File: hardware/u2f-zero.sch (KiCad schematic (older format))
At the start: 13 parts, among them SW1 SW_PUSH

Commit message: add part references
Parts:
- A1: Distributer Link (none) -> http://www.digikey.com/product-detail/en/atmel/ATECC508A-SS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; Distributer PN (none) -> ATECC508A-SSHDA-B-ND; MFG Name (none) -> Atmel; MFG Part Num (none) -> ATECC508A-SSHDA-B
- C3: Distributer Link (none) -> http://www.digikey.com/product-detail/en/CL05A104MP5NNNC/12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; Distributer PN (none) -> 1276-1443-1-ND; MFG Name (none) -> Samsung Electro-Mechanics America, Inc; MFG Part Num (none) -> CL05A104MP5NNNC
- C4: Distributer Link (none) -> http://www.digikey.com/product-detail/en/CL10B475KQ8NQNC/12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; Distributer PN (none) -> 1276-2087-1-ND; MFG Name (none) -> Samsung Electro-Mechanics America, Inc; MFG Part Num (none) -> CL10B475KQ8NQNC
- E0: Distributer Link (none) -> http://www.digikey.com/product-detail/en/silicon-labs/EFM8U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; Distributer PN (none) -> r 336-3411-5-ND; MFG Name (none) -> Silicon Labs; MFG Part Num (none) -> EFM8UB11F16G-C-QSOP24
- R1: Distributer Link (none) -> http://www.digikey.com/product-detail/en/CRCW0603100RFKEA/5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; Distributer PN (none) -> 541-100HCT-ND; MFG Name (none) -> Vishay Dale; MFG Part Num (none) -> CRCW0603100RFKEA
- RGB1: Distributer Link (none) -> http://www.digikey.com/product-detail/en/LTST-C19HE1WT/160-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; Distributer PN (none) -> 160-2162-1-ND; MFG Name (none) -> Lite-On Inc; MFG Part Num (none) -> LTST-C19HE1WT
- SW1: Distributer Link (none) -> http://www.digikey.com/product-detail/en/e-switch/TL3305AF2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; Distributer PN (none) -> EG5353CT-ND; MFG Name (none) -> E-Switch; MFG Part Num (none) -> TL3305AF260QG
- Z1: Distributer Link (none) -> http://www.digikey.com/product-detail/en/DF5A5.6JE,LM/DF5A5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; Distributer PN (none) -> DF5A5.6JELMCT-ND; MFG Name (none) -> Toshiba Semiconductor and Storage; MFG Part Num (none) -> DF5A5.6JE,LM
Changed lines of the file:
@@
 F 2 "Housings_SOIC:SOIC-8_3.9x4.9mm_Pitch1.27mm" H 4700 3300 60  0001 C CNN
 F 3 "http://www.atmel.com/Images/Atmel-8923S-CryptoAuth-ATECC508A-Datasheet-Summary.pdf" H 4700 3300 60  0001 C CNN
+F 4 "Atmel" H 5100 3050 60  0001 C CNN "MFG Name"
+F 5 "ATECC508A-SSHDA-B" H 5100 3050 60  0001 C CNN "MFG Part Num"
+F 6 "ATECC508A-SSHDA-B-ND" H 5100 3050 60  0001 C CNN "Distributer PN"
+F 7 "http://www.digikey.com/product-detail/en/atmel/ATECC508A-SSHDA-B/ATECC508A-SSHDA-B-ND/5213053" H 5100 3050 60  0001 C CNN "Distributer Link"
 	1    5100 3050
 	-1   0    0    1
@@
 F 2 "Capacitors_SMD:C_0402" H 5338 5600 50  0001 C CNN
 F 3 "http://media.digikey.com/pdf/Data%20Sheets/Samsung%20PDFs/CL_Series_MLCC_ds.pdf" H 5300 5750 50  0001 C CNN
+F 4 "Samsung Electro-Mechanics America, Inc" H 5300 5750 60  0001 C CNN "MFG Name"
+F 5 "CL05A104MP5NNNC" H 5300 5750 60  0001 C CNN "MFG Part Num"
+F 6 "1276-1443-1-ND" H 5300 5750 60  0001 C CNN "Distributer PN"
+F 7 "http://www.digikey.com/product-detail/en/CL05A104MP5NNNC/1276-1443-1-ND/3889529" H 5300 5750 60  0001 C CNN "Distributer Link"
 	1    5300 5750
 	0    -1   1    0
@@
 F 2 "Capacitors_SMD:C_0603" H 5338 5950 50  0001 C CNN
 F 3 "http://media.digikey.com/pdf/Data%20Sheets/Samsung%20PDFs/CL_Series_MLCC_ds.pdf" H 5300 6100 50  0001 C CNN
+F 4 "Samsung Electro-Mechanics America, Inc" H 5300 6100 60  0001 C CNN "MFG Name"
+F 5 "CL10B475KQ8NQNC" H 5300 6100 60  0001 C CNN "MFG Part Num"
+F 6 "1276-2087-1-ND" H 5300 6100 60  0001 C CNN "Distributer PN"
+F 7 "http://www.digikey.com/product-detail/en/CL10B475KQ8NQNC/1276-2087-1-ND/3890173" H 5300 6100 60  0001 C CNN "Distributer Link"
 	1    5300 6100
 	0    1    1    0
@@
 F 2 "TO_SOT_Packages_SMD:SOT-553" H 3250 3950 60  0001 C CNN
 F 3 "http://optoelectronics.liteon.com/upload/download/DS22-2008-0044/S_110_LTST-C19HE1WT.pdf" H 3250 3950 60  0001 C CNN
+F 4 "Toshiba Semiconductor and Storage" H 3250 3950 60  0001 C CNN "MFG Name"
+F 5 "DF5A5.6JE,LM" H 3250 3950 60  0001 C CNN "MFG Part Num"
+F 6 "DF5A5.6JELMCT-ND" H 3250 3950 60  0001 C CNN "Distributer PN"
+F 7 "http://www.digikey.com/product-detail/en/DF5A5.6JE,LM/DF5A5.6JELMCT-ND/5403466" H 3250 3950 60  0001 C CNN "Distributer Link"
 	1    3250 3950
 	1    0    0    -1
@@
 F 2 "Resistors_SMD:R_0603" V 8030 4900 50  0001 C CNN
 F 3 "http://www.vishay.com/docs/20035/dcrcwe3.pdf" H 8100 4900 50  0001 C CNN
+F 4 "Vishay Dale" H 8100 4900 60  0001 C CNN "MFG Name"
+F 5 "CRCW0603100RFKEA" H 8100 4900 60  0001 C CNN "MFG Part Num"
+F 6 "541-100HCT-ND" H 8100 4900 60  0001 C CNN "Distributer PN"
+F 7 "http://www.digikey.com/product-detail/en/CRCW0603100RFKEA/541-100HCT-ND/1179695" H 8100 4900 60  0001 C CNN "Distributer Link"
 	1    8100 4900
 	-1   0    0    1
@@
 F 2 "footprints:LED-0606" H 7850 4750 60  0001 C CNN
 F 3 "http://optoelectronics.liteon.com/upload/download/DS22-2008-0044/S_110_LTST-C19HE1WT.pdf" H 7050 4750 60  0001 C CNN
+F 4 "Lite-On Inc" H 7050 4700 60  0001 C CNN "MFG Name"
+F 5 "LTST-C19HE1WT" H 7050 4700 60  0001 C CNN "MFG Part Num"
+F 6 "160-2162-1-ND" H 7050 4700 60  0001 C CNN "Distributer PN"
+F 7 "http://www.digikey.com/product-detail/en/LTST-C19HE1WT/160-2162-1-ND/4866310" H 7050 4700 60  0001 C CNN "Distributer Link"
 	1    7050 4700
 	1    0    0    1
@@
 F 2 "footprints:u2f-button" H 6500 5200 50  0001 C CNN
 F 3 "http://www.digikey.com/product-detail/en/e-switch/TL3305AF260QG/EG5353CT-ND/5816198" H 6500 5200 50  0001 C CNN
+F 4 "E-Switch" H 6500 5200 60  0001 C CNN "MFG Name"
+F 5 "TL3305AF260QG" H 6500 5200 60  0001 C CNN "MFG Part Num"
+F 6 "EG5353CT-ND" H 6500 5200 60  0001 C CNN "Distributer PN"
+F 7 "http://www.digikey.com/product-detail/en/e-switch/TL3305AF260QG/EG5353CT-ND/5816198" H 6500 5200 60  0001 C CNN "Distributer Link"
 	1    6500 5200
 	1    0    0    -1
@@
 F 2 "footprints:QSOP-24_3.9x8.7mm_Pitch0.635mm_fat" H 5650 4650 60  0001 C CNN
 F 3 "https://www.silabs.com/Support%20Documents/TechnicalDocs/EFM8UB1_DataSheet.pdf" H 5350 4250 60  0001 C CNN
+F 4 "Silicon Labs" H 5350 4250 60  0001 C CNN "MFG Name"
+F 5 "EFM8UB11F16G-C-QSOP24" H 5350 4250 60  0001 C CNN "MFG Part Num"
+F 6 "r	336-3411-5-ND" H 5350 4250 60  0001 C CNN "Distributer PN"
+F 7 "http://www.digikey.com/product-detail/en/silicon-labs/EFM8UB11F16G-C-QSOP24/336-3411-5-ND/5592439" H 5350 4250 60  0001 C CNN "Distributer Link"
 	1    5350 4250
 	1    0    0    -1

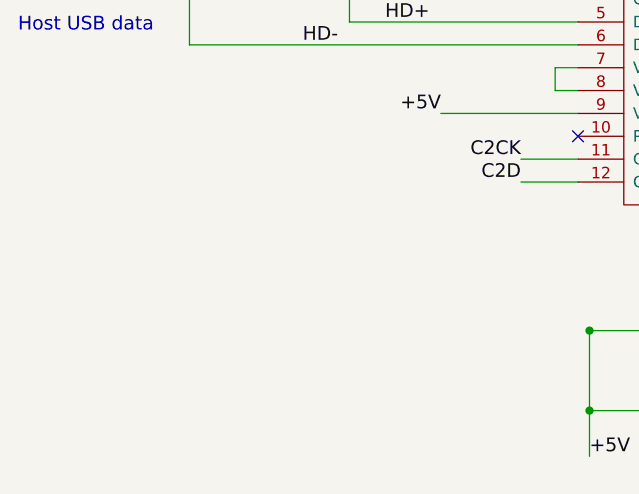
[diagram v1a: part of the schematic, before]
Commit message: add fiducials
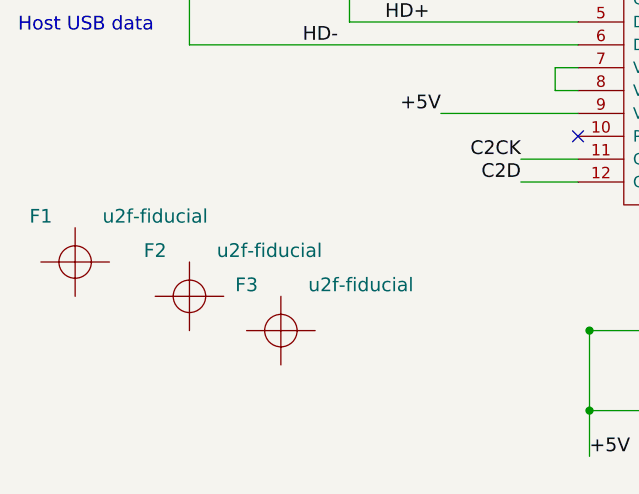
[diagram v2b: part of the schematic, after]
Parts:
- added F1, F2, F3: u2f-fiducial, footprints:u2f-fiducial, symbol u2f-fiducial
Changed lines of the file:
@@
 Wire Wire Line
 	4700 4700 4700 4600
+$Comp
+L u2f-fiducial F1
+U 1 1 571C39BB
+P 2600 5450
+F 0 "F1" H 2450 5650 60  0000 C CNN
+F 1 "u2f-fiducial" H 2950 5650 60  0000 C CNN
+F 2 "footprints:u2f-fiducial" H 2600 5450 60  0001 C CNN
+F 3 "" H 2600 5450 60  0000 C CNN
+	1    2600 5450
+	1    0    0    -1
+$EndComp
+$Comp
+L u2f-fiducial F2
+U 1 1 571C3A1E
+P 3100 5600
+F 0 "F2" H 2950 5800 60  0000 C CNN
+F 1 "u2f-fiducial" H 3450 5800 60  0000 C CNN
+F 2 "footprints:u2f-fiducial" H 3100 5600 60  0001 C CNN
+F 3 "" H 3100 5600 60  0000 C CNN
+	1    3100 5600
+	1    0    0    -1
+$EndComp
+$Comp
+L u2f-fiducial F3
+U 1 1 571C3A85
+P 3500 5750
+F 0 "F3" H 3350 5950 60  0000 C CNN
+F 1 "u2f-fiducial" H 3850 5950 60  0000 C CNN
+F 2 "footprints:u2f-fiducial" H 3500 5750 60  0001 C CNN
+F 3 "" H 3500 5750 60  0000 C CNN
+	1    3500 5750
+	1    0    0    -1
+$EndComp
 $EndSCHEMATC

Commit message: Replace tiny schematic/netlist parts with larger parts.
All passive components: standardized on 0805
TVS diode: currently TSOT-23-5 (could become 6 pins)
LED: 0606 => 5050 (8.3x the horizontal linear size)
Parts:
- C3: footprint Capacitors_SMD:C_0402 -> Capacitors_SMD:C_0805
- C4: footprint Capacitors_SMD:C_0603 -> Capacitors_SMD:C_0805
- R1: footprint Resistors_SMD:R_0603 -> Resistors_SMD:R_0805
- RGB1: footprint footprints:LED-0606 -> LEDs:LED_RGB_5050-6
- Z1: footprint TO_SOT_Packages_SMD:SOT-553 -> TO_SOT_Packages_SMD:TSOT-23-5
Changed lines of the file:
@@
 F 0 "C3" H 5325 5850 50  0000 L CNN
 F 1 "0.1uF" H 5325 5650 50  0000 L CNN
-F 2 "Capacitors_SMD:C_0402" H 5338 5600 50  0001 C CNN
+F 2 "Capacitors_SMD:C_0805" H 5338 5600 50  0001 C CNN
 F 3 "http://media.digikey.com/pdf/Data%20Sheets/Samsung%20PDFs/CL_Series_MLCC_ds.pdf" H 5300 5750 50  0001 C CNN
 F 4 "Samsung Electro-Mechanics America, Inc" H 5300 5750 60  0001 C CNN "MFG Name"
@@
 F 0 "C4" H 5325 6200 50  0000 L CNN
 F 1 "4.7uF" H 5325 6000 50  0000 L CNN
-F 2 "Capacitors_SMD:C_0603" H 5338 5950 50  0001 C CNN
+F 2 "Capacitors_SMD:C_0805" H 5338 5950 50  0001 C CNN
 F 3 "http://media.digikey.com/pdf/Data%20Sheets/Samsung%20PDFs/CL_Series_MLCC_ds.pdf" H 5300 6100 50  0001 C CNN
 F 4 "Samsung Electro-Mechanics America, Inc" H 5300 6100 60  0001 C CNN "MFG Name"
@@
 F 0 "Z1" H 2850 4000 60  0000 C CNN
 F 1 "DF5A5.6JE" H 2700 4100 60  0000 C CNN
-F 2 "TO_SOT_Packages_SMD:SOT-553" H 3250 3950 60  0001 C CNN
+F 2 "TO_SOT_Packages_SMD:TSOT-23-5" H 3250 3950 60  0001 C CNN
 F 3 "http://optoelectronics.liteon.com/upload/download/DS22-2008-0044/S_110_LTST-C19HE1WT.pdf" H 3250 3950 60  0001 C CNN
 F 4 "Toshiba Semiconductor and Storage" H 3250 3950 60  0001 C CNN "MFG Name"
@@
 F 0 "R1" V 8180 4900 50  0000 C CNN
 F 1 "100" V 8100 4900 50  0000 C CNN
-F 2 "Resistors_SMD:R_0603" V 8030 4900 50  0001 C CNN
+F 2 "Resistors_SMD:R_0805" V 8030 4900 50  0001 C CNN
 F 3 "http://www.vishay.com/docs/20035/dcrcwe3.pdf" H 8100 4900 50  0001 C CNN
 F 4 "Vishay Dale" H 8100 4900 60  0001 C CNN "MFG Name"
@@
 F 0 "RGB1" H 7300 4850 60  0000 C CNN
 F 1 "CA_RGB" H 6950 4850 60  0000 C CNN
-F 2 "footprints:LED-0606" H 7850 4750 60  0001 C CNN
+F 2 "LEDs:LED_RGB_5050-6" H 7850 4750 60  0001 C CNN
 F 3 "http://optoelectronics.liteon.com/upload/download/DS22-2008-0044/S_110_LTST-C19HE1WT.pdf" H 7050 4750 60  0001 C CNN
 F 4 "Lite-On Inc" H 7050 4700 60  0001 C CNN "MFG Name"

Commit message: Update for actual physical LED/TVS parts chosen
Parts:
- RGB1: footprint LEDs:LED_RGB_5050-6 -> LEDs:LED_Cree-PLCC4_3.2x2.8mm_CCW; symbol CA_RGB-RESCUE-u2f-zero -> CA_RGB-RESCUE-u2f-zero__Cree
- Z1: footprint TO_SOT_Packages_SMD:TSOT-23-5 -> TO_SOT_Packages_SMD:SOT-353_SC-70-5
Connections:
- net at R1.2: now also RGB1.2 (VCC); no longer RGB1.4 (VCC)
- net at E0.19 (P1.0): now also RGB1.4 (G); no longer RGB1.2 (G)
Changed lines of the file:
@@
 F 0 "Z1" H 2850 4000 60  0000 C CNN
 F 1 "DF5A5.6JE" H 2700 4100 60  0000 C CNN
-F 2 "TO_SOT_Packages_SMD:TSOT-23-5" H 3250 3950 60  0001 C CNN
+F 2 "TO_SOT_Packages_SMD:SOT-353_SC-70-5" H 3250 3950 60  0001 C CNN
 F 3 "http://optoelectronics.liteon.com/upload/download/DS22-2008-0044/S_110_LTST-C19HE1WT.pdf" H 3250 3950 60  0001 C CNN
 F 4 "Toshiba Semiconductor and Storage" H 3250 3950 60  0001 C CNN "MFG Name"
@@
 Secure element for EC
 $Comp
-L CA_RGB-RESCUE-u2f-zero RGB1
+L CA_RGB-RESCUE-u2f-zero__Cree RGB1
 U 1 1 5686DEFD
 P 7050 4700
 F 0 "RGB1" H 7300 4850 60  0000 C CNN
 F 1 "CA_RGB" H 6950 4850 60  0000 C CNN
-F 2 "LEDs:LED_RGB_5050-6" H 7850 4750 60  0001 C CNN
+F 2 "LEDs:LED_Cree-PLCC4_3.2x2.8mm_CCW" H 7850 4750 60  0001 C CNN
 F 3 "http://optoelectronics.liteon.com/upload/download/DS22-2008-0044/S_110_LTST-C19HE1WT.pdf" H 7050 4750 60  0001 C CNN
 F 4 "Lite-On Inc" H 7050 4700 60  0001 C CNN "MFG Name"

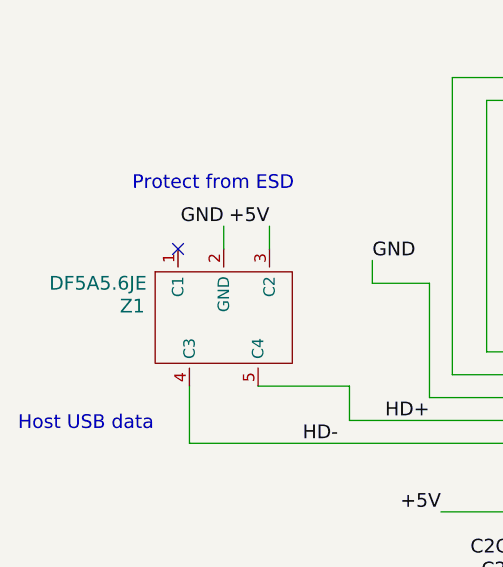
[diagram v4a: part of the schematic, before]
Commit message: Update the BOM csv with new values matching the larger footprints
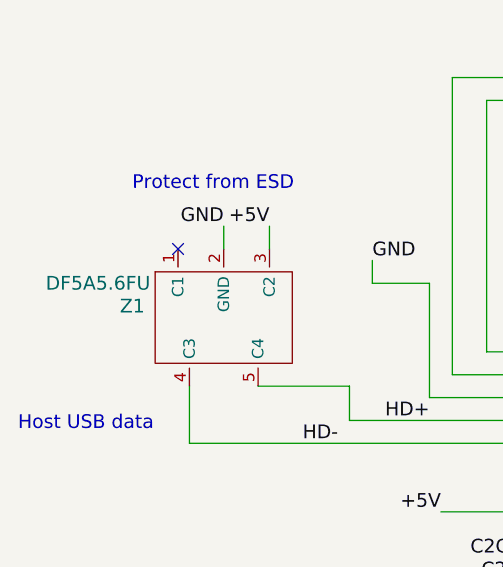
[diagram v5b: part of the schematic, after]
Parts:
- C3: Distributer Link http://www.digikey.com/product-detail/en/CL05A104MP5NNNC/12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 -> https://www.digikey.com/product-detail/en/murata-electronic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; Distributer PN 1276-1443-1-ND -> 490-12558-1-ND; MFG Name Samsung Electro-Mechanics America, Inc -> Murata Manufacturing Co., Ltd.; MFG Part Num CL05A104MP5NNNC -> GRM219R71C104MA01J
- C4: Distributer Link http://www.digikey.com/product-detail/en/CL10B475KQ8NQNC/12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 -> https://www.digikey.com/product-detail/en/murata-electronic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; Distributer PN 1276-2087-1-ND -> 490-14466-1-ND; MFG Name Samsung Electro-Mechanics America, Inc -> Murata Manufacturing Co., Ltd.; MFG Part Num CL10B475KQ8NQNC -> GRM21BR71C475KE51L
- R1: Distributer Link http://www.digikey.com/product-detail/en/CRCW0603100RFKEA/5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 -> https://www.digikey.com/product-detail/en/vishay-dale/CRCW0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; Distributer PN 541-100HCT-ND -> 541-100CCT-ND; MFG Part Num CRCW0603100RFKEA -> CRCW0805100RFKEA
- RGB1: Distributer Link http://www.digikey.com/product-detail/en/LTST-C19HE1WT/160-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 -> https://www.digikey.com/product-detail/en/cree-inc/CLVBA-FK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; Distributer PN 160-2162-1-ND -> CLVBA-FKA-CAEDH8BBB7A363CT-ND; MFG Name Lite-On Inc -> Cree; MFG Part Num LTST-C19HE1WT -> CLVBA-FKA
- Z1: value DF5A5.6JE -> DF5A5.6FU; Distributer Link http://www.digikey.com/product-detail/en/DF5A5.6JE,LM/DF5A5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 -> https://www.digikey.com/product-detail/en/toshiba-semicondu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; Distributer PN DF5A5.6JELMCT-ND -> DF5A5.6FUTE85LFCT-ND; MFG Part Num DF5A5.6JE,LM -> DF5A5.6FUTE85LF
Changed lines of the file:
@@
 F 1 "0.1uF" H 5325 5650 50  0000 L CNN
 F 2 "Capacitors_SMD:C_0805" H 5338 5600 50  0001 C CNN
-F 3 "http://media.digikey.com/pdf/Data%20Sheets/Samsung%20PDFs/CL_Series_MLCC_ds.pdf" H 5300 5750 50  0001 C CNN
-F 4 "Samsung Electro-Mechanics America, Inc" H 5300 5750 60  0001 C CNN "MFG Name"
-F 5 "CL05A104MP5NNNC" H 5300 5750 60  0001 C CNN "MFG Part Num"
-F 6 "1276-1443-1-ND" H 5300 5750 60  0001 C CNN "Distributer PN"
-F 7 "http://www.digikey.com/product-detail/en/CL05A104MP5NNNC/1276-1443-1-ND/3889529" H 5300 5750 60  0001 C CNN "Distributer Link"
+F 3 "https://search.murata.co.jp/Ceramy/image/img/A01X/G101/ENG/GRM219R71C104MA01-01.pdf" H 5300 5750 50  0001 C CNN
+F 4 "Murata Manufacturing Co., Ltd." H 5300 5750 60  0001 C CNN "MFG Name"
+F 5 "GRM219R71C104MA01J" H 5300 5750 60  0001 C CNN "MFG Part Num"
+F 6 "490-12558-1-ND" H 5300 5750 60  0001 C CNN "Distributer PN"
+F 7 "https://www.digikey.com/product-detail/en/murata-electronics-north-america/GRM219R71C104MA01J/490-12558-1-ND/5797548" H 5300 5750 60  0001 C CNN "Distributer Link"
 	1    5300 5750
 	0    -1   1    0
@@
 F 1 "4.7uF" H 5325 6000 50  0000 L CNN
 F 2 "Capacitors_SMD:C_0805" H 5338 5950 50  0001 C CNN
-F 3 "http://media.digikey.com/pdf/Data%20Sheets/Samsung%20PDFs/CL_Series_MLCC_ds.pdf" H 5300 6100 50  0001 C CNN
-F 4 "Samsung Electro-Mechanics America, Inc" H 5300 6100 60  0001 C CNN "MFG Name"
-F 5 "CL10B475KQ8NQNC" H 5300 6100 60  0001 C CNN "MFG Part Num"
-F 6 "1276-2087-1-ND" H 5300 6100 60  0001 C CNN "Distributer PN"
-F 7 "http://www.digikey.com/product-detail/en/CL10B475KQ8NQNC/1276-2087-1-ND/3890173" H 5300 6100 60  0001 C CNN "Distributer Link"
+F 3 "https://search.murata.co.jp/Ceramy/image/img/A01X/G101/ENG/GRM21BR71C475KE51-01.pdf" H 5300 6100 50  0001 C CNN
+F 4 "Murata Manufacturing Co., Ltd." H 5300 6100 60  0001 C CNN "MFG Name"
+F 5 "GRM21BR71C475KE51L" H 5300 6100 60  0001 C CNN "MFG Part Num"
+F 6 "490-14466-1-ND" H 5300 6100 60  0001 C CNN "Distributer PN"
+F 7 "https://www.digikey.com/product-detail/en/murata-electronics-north-america/GRM21BR71C475KE51L/490-14466-1-ND/6606927" H 5300 6100 60  0001 C CNN "Distributer Link"
 	1    5300 6100
 	0    1    1    0
@@
 P 3250 3950
 F 0 "Z1" H 2850 4000 60  0000 C CNN
-F 1 "DF5A5.6JE" H 2700 4100 60  0000 C CNN
+F 1 "DF5A5.6FU" H 2700 4100 60  0000 C CNN
 F 2 "TO_SOT_Packages_SMD:SOT-353_SC-70-5" H 3250 3950 60  0001 C CNN
-F 3 "http://optoelectronics.liteon.com/upload/download/DS22-2008-0044/S_110_LTST-C19HE1WT.pdf" H 3250 3950 60  0001 C CNN
+F 3 "https://toshiba.semicon-storage.com/info/docget.jsp?did=22252&prodName=DF5A5.6FU" H 3250 3950 60  0001 C CNN
 F 4 "Toshiba Semiconductor and Storage" H 3250 3950 60  0001 C CNN "MFG Name"
-F 5 "DF5A5.6JE,LM" H 3250 3950 60  0001 C CNN "MFG Part Num"
-F 6 "DF5A5.6JELMCT-ND" H 3250 3950 60  0001 C CNN "Distributer PN"
-F 7 "http://www.digikey.com/product-detail/en/DF5A5.6JE,LM/DF5A5.6JELMCT-ND/5403466" H 3250 3950 60  0001 C CNN "Distributer Link"
+F 5 "DF5A5.6FUTE85LF" H 3250 3950 60  0001 C CNN "MFG Part Num"
+F 6 "DF5A5.6FUTE85LFCT-ND" H 3250 3950 60  0001 C CNN "Distributer PN"
+F 7 "https://www.digikey.com/product-detail/en/toshiba-semiconductor-and-storage/DF5A5.6FUTE85LF/DF5A5.6FUTE85LFCT-ND/4304119" H 3250 3950 60  0001 C CNN "Distributer Link"
 	1    3250 3950
 	1    0    0    -1
@@
 F 3 "http://www.vishay.com/docs/20035/dcrcwe3.pdf" H 8100 4900 50  0001 C CNN
 F 4 "Vishay Dale" H 8100 4900 60  0001 C CNN "MFG Name"
-F 5 "CRCW0603100RFKEA" H 8100 4900 60  0001 C CNN "MFG Part Num"
-F 6 "541-100HCT-ND" H 8100 4900 60  0001 C CNN "Distributer PN"
-F 7 "http://www.digikey.com/product-detail/en/CRCW0603100RFKEA/541-100HCT-ND/1179695" H 8100 4900 60  0001 C CNN "Distributer Link"
+F 5 "CRCW0805100RFKEA" H 8100 4900 60  0001 C CNN "MFG Part Num"
+F 6 "541-100CCT-ND" H 8100 4900 60  0001 C CNN "Distributer PN"
+F 7 "https://www.digikey.com/product-detail/en/vishay-dale/CRCW0805100RFKEA/541-100CCT-ND/1180669" H 8100 4900 60  0001 C CNN "Distributer Link"
 	1    8100 4900
 	-1   0    0    1
@@
 F 1 "CA_RGB" H 6950 4850 60  0000 C CNN
 F 2 "LEDs:LED_Cree-PLCC4_3.2x2.8mm_CCW" H 7850 4750 60  0001 C CNN
-F 3 "http://optoelectronics.liteon.com/upload/download/DS22-2008-0044/S_110_LTST-C19HE1WT.pdf" H 7050 4750 60  0001 C CNN
-F 4 "Lite-On Inc" H 7050 4700 60  0001 C CNN "MFG Name"
-F 5 "LTST-C19HE1WT" H 7050 4700 60  0001 C CNN "MFG Part Num"
-F 6 "160-2162-1-ND" H 7050 4700 60  0001 C CNN "Distributer PN"
-F 7 "http://www.digikey.com/product-detail/en/LTST-C19HE1WT/160-2162-1-ND/4866310" H 7050 4700 60  0001 C CNN "Distributer Link"
+F 3 "http://www.cree.com/led-components/media/documents/ds-CLVBA-FKA.pdf" H 7050 4750 60  0001 C CNN
+F 4 "Cree" H 7050 4700 60  0001 C CNN "MFG Name"
+F 5 "CLVBA-FKA" H 7050 4700 60  0001 C CNN "MFG Part Num"
+F 6 "CLVBA-FKA-CAEDH8BBB7A363CT-ND" H 7050 4700 60  0001 C CNN "Distributer PN"
+F 7 "https://www.digikey.com/product-detail/en/cree-inc/CLVBA-FKA-CAEDH8BBB7A363/CLVBA-FKA-CAEDH8BBB7A363CT-ND/2650500" H 7050 4700 60  0001 C CNN "Distributer Link"
 	1    7050 4700
 	1    0    0    1
